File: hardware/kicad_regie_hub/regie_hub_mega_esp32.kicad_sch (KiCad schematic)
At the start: 11 parts

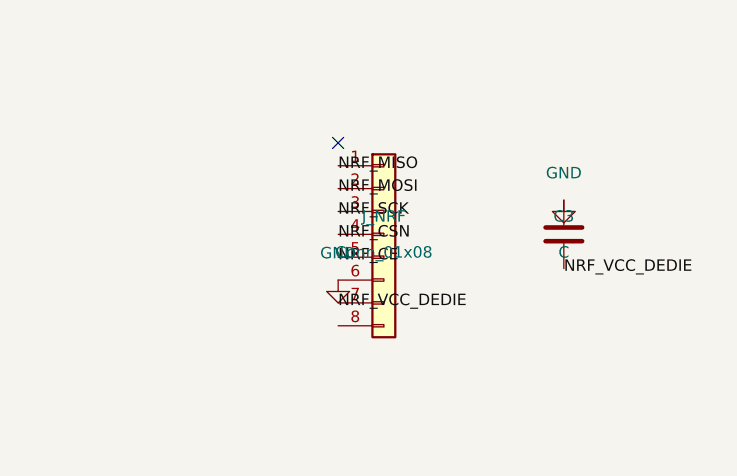
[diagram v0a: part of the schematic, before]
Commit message: hardware: corrige VCC/GND nRF24 (inverses) + passe en 2x4 (module PA+LNA)
En reponse a "le nrf24 c'est sur une ligne ?", verification du brochage
nRF24 contre 3 sources independantes (components101.com,
lastminuteengineers.com, doc generale nRF24L01+) : la broche 1 est GND et
la broche 2 est VCC, pas l'inverse comme c'etait cable jusqu'ici sur J1
(carte Nano) et J_NRF (carte hub) -- schema ET PCB. Broche 1 = toujours la
pastille carree sur cette empreinte, coherent avec "GND identifiable par
son marquage carre" documente pour ce module.

Le module confirme etant un nRF24L01+PA+LNA (longue portee), son connecteur
est 2x4 et non 1x8 standard -- empreinte changee vers PinSocket_2x04 sur
les 2 cartes concernees, brochage 1=GND 2=VCC puis CE/CSN/SCK/MOSI/MISO/IRQ
sur les rangees suivantes (ordre le plus courant publie, mais AUCUN
standard universel n'existe pour les variantes PA+LNA -- avertissement
explicite dans le README et sur la serigraphie: verifier sur le module
recu avant de souder).

Schemas re-verifies (kicad-cli sch erc, memes comptes qu'avant -- aucune
regression). PCB re-routes (Freerouting) et revalides (kicad-cli pcb drc):
0 violation de clearance, 0 element non connecte, 0 track_dangling.

Co-Authored-By: Claude Sonnet 5 <noreply@anthropic.com>
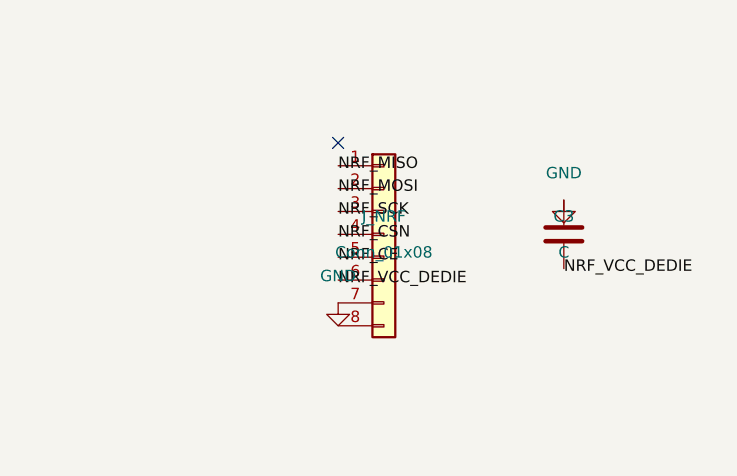
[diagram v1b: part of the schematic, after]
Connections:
- net GND: now also J_NRF.7 (Pin_7); no longer J_NRF.6 (Pin_6)
- net NRF_VCC_DEDIE: now also J_NRF.6 (Pin_6); no longer J_NRF.7 (Pin_7)
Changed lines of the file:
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@@
     (instances
       (project "regie_hub_mega_esp32"
-        (path "/30720212-6308-490c-a58d-90dc739adcc3"
+        (path "/e13100e9-89d9-4d1a-a7b7-703f7a0a45ce"
           (reference "J_MEGA")
           (unit 1)
@@
     (instances
       (project "regie_hub_mega_esp32"
-        (path "/30720212-6308-490c-a58d-90dc739adcc3"
+        (path "/e13100e9-89d9-4d1a-a7b7-703f7a0a45ce"
           (reference "U_ESP32")
           (unit 1)
@@
     (instances
       (project "regie_hub_mega_esp32"
-        (path "/30720212-6308-490c-a58d-90dc739adcc3"
+        (path "/e13100e9-89d9-4d1a-a7b7-703f7a0a45ce"
           (reference "J_NRF")
           (unit 1)
@@
     (instances
       (project "regie_hub_mega_esp32"
-        (path "/30720212-6308-490c-a58d-90dc739adcc3"
+        (path "/e13100e9-89d9-4d1a-a7b7-703f7a0a45ce"
           (reference "U_REG")
           (unit 1)
@@
     (instances
       (project "regie_hub_mega_esp32"
-        (path "/30720212-6308-490c-a58d-90dc739adcc3"
+        (path "/e13100e9-89d9-4d1a-a7b7-703f7a0a45ce"
           (reference "R1")
           (unit 1)
@@
     (instances
       (project "regie_hub_mega_esp32"
-        (path "/30720212-6308-490c-a58d-90dc739adcc3"
+        (path "/e13100e9-89d9-4d1a-a7b7-703f7a0a45ce"
           (reference "R2")
           (unit 1)
@@
     (instances
       (project "regie_hub_mega_esp32"
-        (path "/30720212-6308-490c-a58d-90dc739adcc3"
+        (path "/e13100e9-89d9-4d1a-a7b7-703f7a0a45ce"
           (reference "R3")
           (unit 1)
@@
     (instances
       (project "regie_hub_mega_esp32"
-        (path "/30720212-6308-490c-a58d-90dc739adcc3"
+        (path "/e13100e9-89d9-4d1a-a7b7-703f7a0a45ce"
           (reference "R4")
           (unit 1)
@@
     (instances
       (project "regie_hub_mega_esp32"
-        (path "/30720212-6308-490c-a58d-90dc739adcc3"
+        (path "/e13100e9-89d9-4d1a-a7b7-703f7a0a45ce"
           (reference "C1")
           (unit 1)
@@
     (instances
       (project "regie_hub_mega_esp32"
-        (path "/30720212-6308-490c-a58d-90dc739adcc3"
+        (path "/e13100e9-89d9-4d1a-a7b7-703f7a0a45ce"
           (reference "C2")
           (unit 1)
@@
     (instances
       (project "regie_hub_mega_esp32"
-        (path "/30720212-6308-490c-a58d-90dc739adcc3"
+        (path "/e13100e9-89d9-4d1a-a7b7-703f7a0a45ce"
           (reference "C3")
           (unit 1)
@@
     (instances
       (project "regie_hub_mega_esp32"
-        (path "/30720212-6308-490c-a58d-90dc739adcc3"
+        (path "/e13100e9-89d9-4d1a-a7b7-703f7a0a45ce"
           (reference "#PWRGND00")
           (unit 1)
@@
     (instances
       (project "regie_hub_mega_esp32"
-        (path "/30720212-6308-490c-a58d-90dc739adcc3"
+        (path "/e13100e9-89d9-4d1a-a7b7-703f7a0a45ce"
           (reference "#PWRGND01")
           (unit 1)
@@
   (symbol
     (lib_id "power:GND")
-    (at 164.92 105.08 0)
+    (at 164.92 107.62 0)
     (unit 1)
     (exclude_from_sim no)
@@
     (dnp no)
     (property "Reference" "#PWRGND02"
-      (at 164.92 100.08 0)
+      (at 164.92 102.62 0)
       (effects (font (size 1.27 1.27)) hide)
     )
     (property "Value" "GND"
-      (at 164.92 102.08 0)
-      (effects (font (size 1.27 1.27)))
-    )
-    (property "Footprint" ""
-      (at 164.92 105.08 0)
-      (effects (font (size 1.27 1.27)) hide)
-    )
-    (property "Datasheet" "~"
-      (at 164.92 105.08 0)
-      (effects (font (size 1.27 1.27)) hide)
-    )
-    (property "Description" ""
-      (at 164.92 105.08 0)
+      (at 164.92 104.62 0)
+      (effects (font (size 1.27 1.27)))
+    )
+    (property "Footprint" ""
+      (at 164.92 107.62 0)
+      (effects (font (size 1.27 1.27)) hide)
+    )
+    (property "Datasheet" "~"
+      (at 164.92 107.62 0)
+      (effects (font (size 1.27 1.27)) hide)
+    )
+    (property "Description" ""
+      (at 164.92 107.62 0)
       (effects (font (size 1.27 1.27)) hide)
     )
@@
     (instances
       (project "regie_hub_mega_esp32"
-        (path "/30720212-6308-490c-a58d-90dc739adcc3"
+        (path "/e13100e9-89d9-4d1a-a7b7-703f7a0a45ce"
           (reference "#PWRGND02")
           (unit 1)
@@
     (instances
       (project "regie_hub_mega_esp32"
-        (path "/30720212-6308-490c-a58d-90dc739adcc3"
+        (path "/e13100e9-89d9-4d1a-a7b7-703f7a0a45ce"
           (reference "#PWRGND03")
           (unit 1)
@@
     (instances
       (project "regie_hub_mega_esp32"
-        (path "/30720212-6308-490c-a58d-90dc739adcc3"
+        (path "/e13100e9-89d9-4d1a-a7b7-703f7a0a45ce"
           (reference "#PWRGND04")
           (unit 1)
@@
     (instances
       (project "regie_hub_mega_esp32"
-        (path "/30720212-6308-490c-a58d-90dc739adcc3"
+        (path "/e13100e9-89d9-4d1a-a7b7-703f7a0a45ce"
           (reference "#PWRGND05")
           (unit 1)
@@
     (instances
       (project "regie_hub_mega_esp32"
-        (path "/30720212-6308-490c-a58d-90dc739adcc3"
+        (path "/e13100e9-89d9-4d1a-a7b7-703f7a0a45ce"
           (reference "#PWRGND06")
           (unit 1)
@@
     (instances
       (project "regie_hub_mega_esp32"
-        (path "/30720212-6308-490c-a58d-90dc739adcc3"
+        (path "/e13100e9-89d9-4d1a-a7b7-703f7a0a45ce"
           (reference "#PWRGND07")
           (unit 1)
@@
     (instances
       (project "regie_hub_mega_esp32"
-        (path "/30720212-6308-490c-a58d-90dc739adcc3"
+        (path "/e13100e9-89d9-4d1a-a7b7-703f7a0a45ce"
           (reference "#PWRGND08")
           (unit 1)
@@
   )
   (label "NRF_VCC_DEDIE"
-    (at 164.92 107.62 0)
+    (at 164.92 105.08 0)
     (effects (font (size 1.27 1.27)) (justify left))
   )
